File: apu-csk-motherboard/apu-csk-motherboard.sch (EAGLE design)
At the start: 11 parts

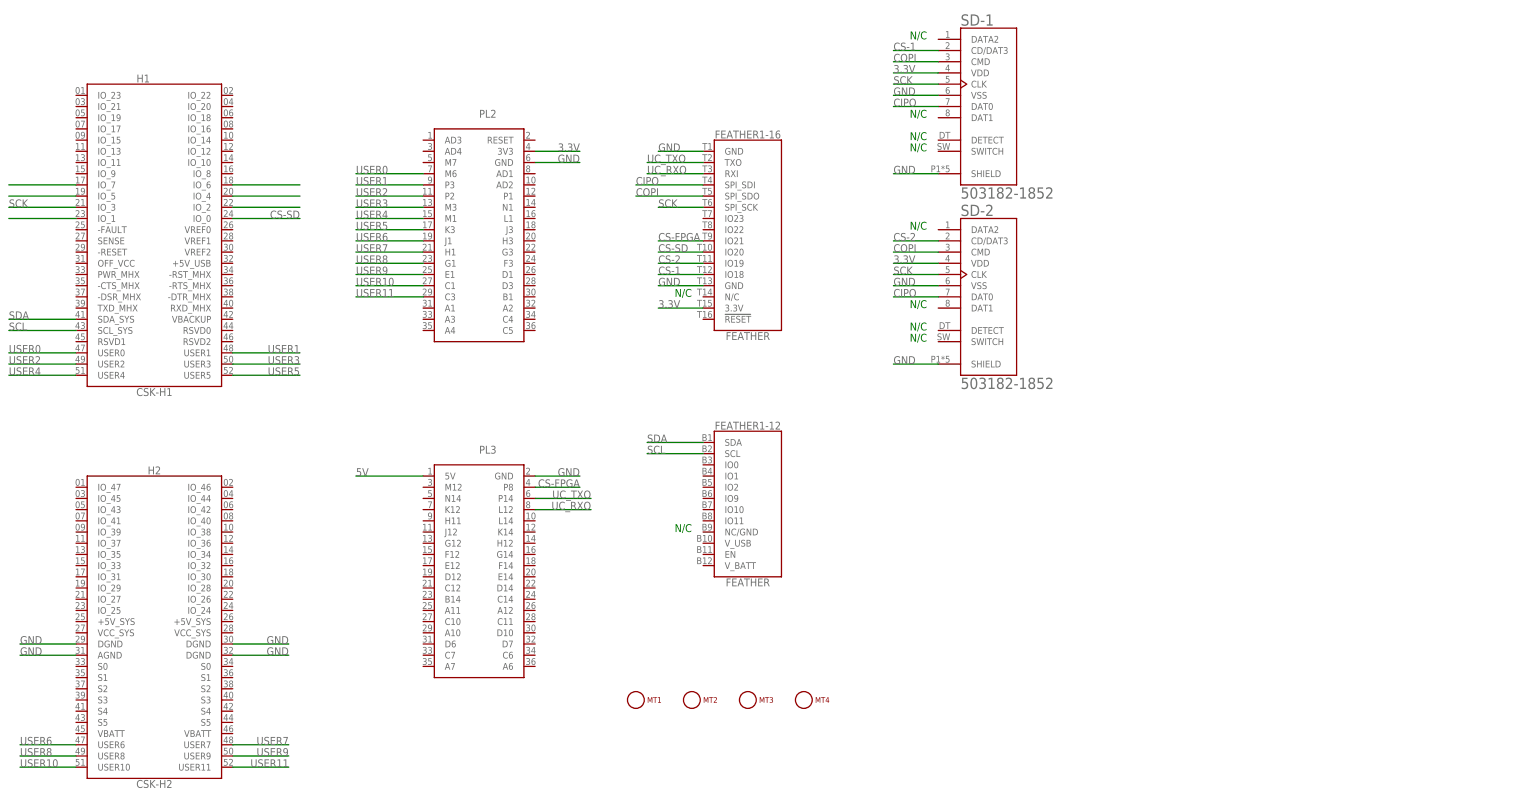
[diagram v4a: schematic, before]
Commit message: Added 4 temperature sensors, Authenitcation Chip, and Conncetors for RBF Switch
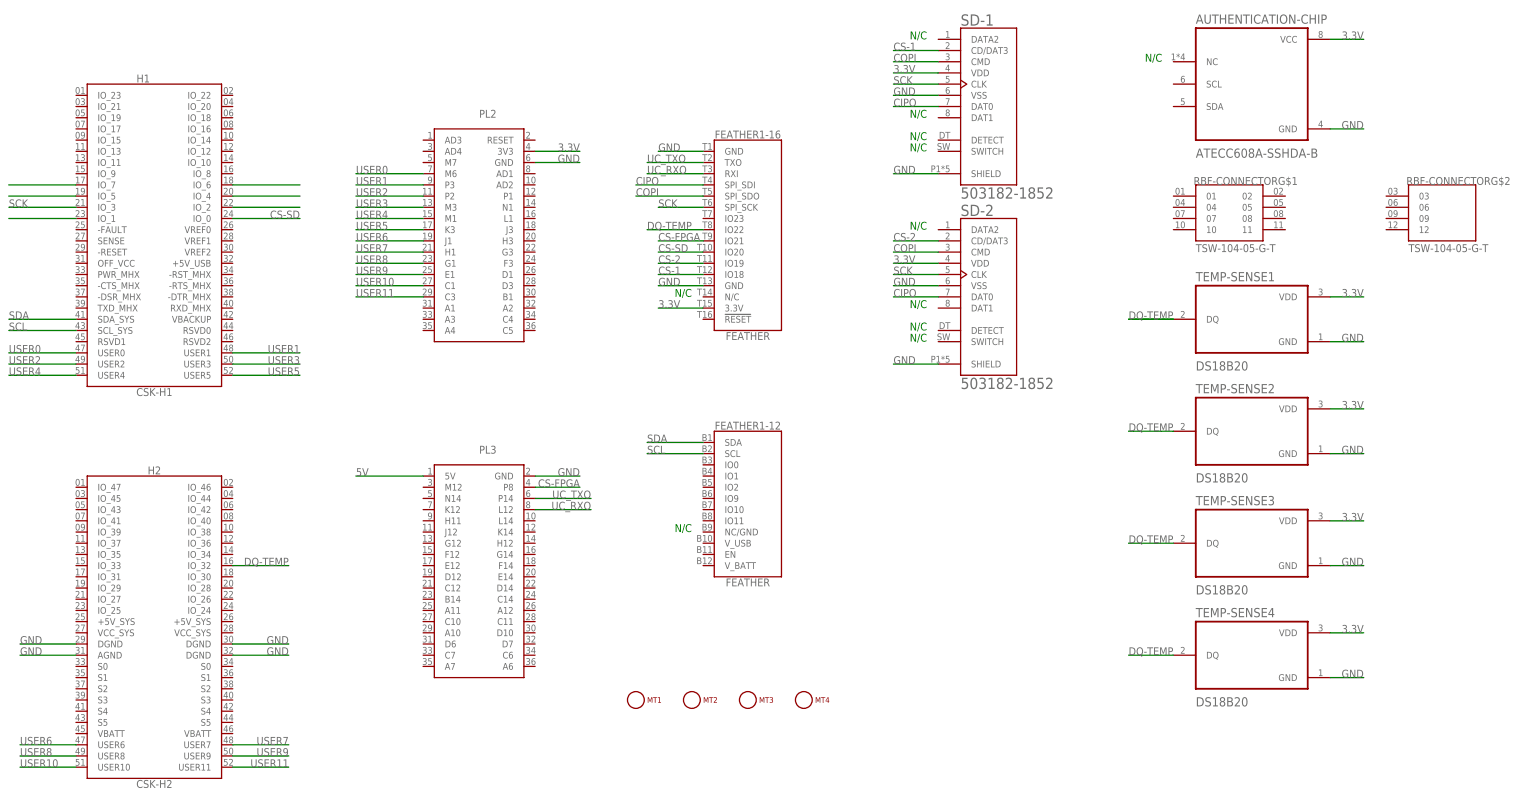
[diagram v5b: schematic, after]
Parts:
- added AUTHENTICATION-CHIP: ATECC608A-SSHDA-B, ATECC608A-SSHDA-B:ATECC608A-SSHDA-B
- added RBF-CONNECTOR: TSW-104-05-G-T, TSW-104-05-G-T:TSW-104-05-G-T
- added TEMP-SENSE1, TEMP-SENSE2, TEMP-SENSE3, TEMP-SENSE4: DS18B20, DS18B20:DS18B20
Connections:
- new net DQ-TEMP: FEATHER1-16.IO22@T8, H2.IO_32@16, TEMP-SENSE1.DQ, TEMP-SENSE2.DQ, TEMP-SENSE3.DQ, TEMP-SENSE4.DQ
- net 3.3V: now also AUTHENTICATION-CHIP.VCC, TEMP-SENSE1.VDD, TEMP-SENSE2.VDD, TEMP-SENSE3.VDD, TEMP-SENSE4.VDD
- net GND: now also AUTHENTICATION-CHIP.GND, TEMP-SENSE1.GND, TEMP-SENSE2.GND, TEMP-SENSE3.GND, TEMP-SENSE4.GND
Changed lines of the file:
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@@
 <part name="SD-1" library="503182-1852" deviceset="503182-1852" device=""/>
 <part name="SD-2" library="503182-1852" deviceset="503182-1852" device=""/>
+<part name="FRAME2" library="apu-csk-motherboard" deviceset="FRAME_LETTER_LANDSCAPE" device=""/>
+<part name="AUTHENTICATION-CHIP" library="ATECC608A-SSHDA-B" deviceset="ATECC608A-SSHDA-B" device=""/>
+<part name="RBF-CONNECTOR" library="TSW-104-05-G-T" deviceset="TSW-104-05-G-T" device=""/>
+<part name="TEMP-SENSE1" library="DS18B20" deviceset="DS18B20" device=""/>
+<part name="TEMP-SENSE2" library="DS18B20" deviceset="DS18B20" device=""/>
+<part name="TEMP-SENSE3" library="DS18B20" deviceset="DS18B20" device=""/>
+<part name="TEMP-SENSE4" library="DS18B20" deviceset="DS18B20" device=""/>
 </parts>
 <sheets>
@@
 <text x="218.44" y="114.3" size="1.778" layer="91" rot="MR0">N/C</text>
 <text x="218.44" y="111.76" size="1.778" layer="91" rot="MR0">N/C</text>
+<text x="271.78" y="175.26" size="1.778" layer="91" rot="MR0">N/C</text>
 </plain>
 <instances>
@@
 <attribute name="VALUE" x="226.06" y="101.025" size="2.548159375" layer="96"/>
 </instance>
+<instance part="FRAME2" gate="G$2" x="408.94" y="2.54" smashed="yes">
+<attribute name="LAST_DATE_TIME" x="421.64" y="3.81" size="2.54" layer="94"/>
+<attribute name="SHEET" x="495.3" y="3.81" size="2.54" layer="94"/>
+<attribute name="DRAWING_NAME" x="426.72" y="21.59" size="2.54" layer="94"/>
+</instance>
+<instance part="FRAME2" gate="G$1" x="261.62" y="2.54" smashed="yes"/>
+<instance part="AUTHENTICATION-CHIP" gate="G$1" x="292.1" y="170.18" smashed="yes">
+<attribute name="NAME" x="279.4" y="183.88" size="2.0828" layer="95" ratio="10" rot="SR0"/>
+<attribute name="VALUE" x="279.4" y="153.48" size="2.0828" layer="96" ratio="10" rot="SR0"/>
+</instance>
+<instance part="RBF-CONNECTOR" gate="G$1" x="287.02" y="139.7" smashed="yes">
+<attribute name="NAME" x="278.9" y="147.32" size="1.778" layer="95"/>
+<attribute name="VALUE" x="279.4" y="132.08" size="1.778" layer="96"/>
+</instance>
+<instance part="RBF-CONNECTOR" gate="G$2" x="335.28" y="139.7" smashed="yes">
+<attribute name="NAME" x="327.16" y="147.32" size="1.778" layer="95"/>
+<attribute name="VALUE" x="327.66" y="132.08" size="1.778" layer="96"/>
+</instance>
+<instance part="TEMP-SENSE1" gate="G$1" x="292.1" y="116.84" smashed="yes">
+<attribute name="NAME" x="279.4" y="125.46" size="2.0828" layer="95" ratio="10" rot="SR0"/>
+<attribute name="VALUE" x="279.4" y="105.22" size="2.0828" layer="96" ratio="10" rot="SR0"/>
+</instance>
+<instance part="TEMP-SENSE2" gate="G$1" x="292.1" y="91.44" smashed="yes">
+<attribute name="NAME" x="279.4" y="100.06" size="2.0828" layer="95" ratio="10" rot="SR0"/>
+<attribute name="VALUE" x="279.4" y="79.82" size="2.0828" layer="96" ratio="10" rot="SR0"/>
+</instance>
+<instance part="TEMP-SENSE3" gate="G$1" x="292.1" y="66.04" smashed="yes">
+<attribute name="NAME" x="279.4" y="74.66" size="2.0828" layer="95" ratio="10" rot="SR0"/>
+<attribute name="VALUE" x="279.4" y="54.42" size="2.0828" layer="96" ratio="10" rot="SR0"/>
+</instance>
+<instance part="TEMP-SENSE4" gate="G$1" x="292.1" y="40.64" smashed="yes">
+<attribute name="NAME" x="279.4" y="49.26" size="2.0828" layer="95" ratio="10" rot="SR0"/>
+<attribute name="VALUE" x="279.4" y="29.02" size="2.0828" layer="96" ratio="10" rot="SR0"/>
+</instance>
 </instances>
 <busses>
@@
 <label x="210.82" y="167.64" size="1.778" layer="95"/>
 </segment>
+<segment>
+<pinref part="TEMP-SENSE4" gate="G$1" pin="GND"/>
+<wire x1="317.5" y1="35.56" x2="309.88" y2="35.56" width="0.1524" layer="91"/>
+<label x="317.5" y="35.56" size="1.778" layer="95" rot="MR0"/>
+</segment>
+<segment>
+<pinref part="TEMP-SENSE3" gate="G$1" pin="GND"/>
+<wire x1="317.5" y1="60.96" x2="309.88" y2="60.96" width="0.1524" layer="91"/>
+<label x="317.5" y="60.96" size="1.778" layer="95" rot="MR0"/>
+</segment>
+<segment>
+<pinref part="TEMP-SENSE2" gate="G$1" pin="GND"/>
+<wire x1="317.5" y1="86.36" x2="309.88" y2="86.36" width="0.1524" layer="91"/>
+<label x="317.5" y="86.36" size="1.778" layer="95" rot="MR0"/>
+</segment>
+<segment>
+<pinref part="TEMP-SENSE1" gate="G$1" pin="GND"/>
+<wire x1="317.5" y1="111.76" x2="309.88" y2="111.76" width="0.1524" layer="91"/>
+<label x="317.5" y="111.76" size="1.778" layer="95" rot="MR0"/>
+</segment>
+<segment>
+<pinref part="AUTHENTICATION-CHIP" gate="G$1" pin="GND"/>
+<wire x1="317.5" y1="160.02" x2="309.88" y2="160.02" width="0.1524" layer="91"/>
+<label x="317.5" y="160.02" size="1.778" layer="95" rot="MR0"/>
+</segment>
 </net>
 <net name="3.3V" class="0">
@@
 <label x="210.82" y="172.72" size="1.778" layer="95"/>
 </segment>
+<segment>
+<pinref part="TEMP-SENSE1" gate="G$1" pin="VDD"/>
+<wire x1="309.88" y1="121.92" x2="317.5" y2="121.92" width="0.1524" layer="91"/>
+<label x="317.5" y="121.92" size="1.778" layer="95" rot="MR0"/>
+</segment>
+<segment>
+<pinref part="TEMP-SENSE2" gate="G$1" pin="VDD"/>
+<wire x1="317.5" y1="96.52" x2="309.88" y2="96.52" width="0.1524" layer="91"/>
+<label x="317.5" y="96.52" size="1.778" layer="95" rot="MR0"/>
+</segment>
+<segment>
+<pinref part="TEMP-SENSE3" gate="G$1" pin="VDD"/>
+<wire x1="317.5" y1="71.12" x2="309.88" y2="71.12" width="0.1524" layer="91"/>
+<label x="317.5" y="71.12" size="1.778" layer="95" rot="MR0"/>
+</segment>
+<segment>
+<pinref part="TEMP-SENSE4" gate="G$1" pin="VDD"/>
+<wire x1="317.5" y1="45.72" x2="309.88" y2="45.72" width="0.1524" layer="91"/>
+<label x="317.5" y="45.72" size="1.778" layer="95" rot="MR0"/>
+</segment>
+<segment>
+<pinref part="AUTHENTICATION-CHIP" gate="G$1" pin="VCC"/>
+<wire x1="317.5" y1="180.34" x2="309.88" y2="180.34" width="0.1524" layer="91"/>
+<label x="317.5" y="180.34" size="1.778" layer="95" rot="MR0"/>
+</segment>
 </net>
 <net name="SDA" class="0">
@@
 </segment>
 </net>
+<net name="DQ-TEMP" class="0">
+<segment>
+<pinref part="TEMP-SENSE1" gate="G$1" pin="DQ"/>
+<wire x1="264.16" y1="116.84" x2="274.32" y2="116.84" width="0.1524" layer="91"/>
+<label x="264.16" y="116.84" size="1.778" layer="95"/>
+<wire x1="264.16" y1="116.84" x2="274.32" y2="116.84" width="0.1524" layer="91"/>
+</segment>
+<segment>
+<pinref part="TEMP-SENSE2" gate="G$1" pin="DQ"/>
+<wire x1="264.16" y1="91.44" x2="274.32" y2="91.44" width="0.1524" layer="91"/>
+<label x="264.16" y="91.44" size="1.778" layer="95"/>
+</segment>
+<segment>
+<pinref part="TEMP-SENSE3" gate="G$1" pin="DQ"/>
+<wire x1="264.16" y1="66.04" x2="274.32" y2="66.04" width="0.1524" layer="91"/>
+<label x="264.16" y="66.04" size="1.778" layer="95"/>
+</segment>
+<segment>
+<pinref part="TEMP-SENSE4" gate="G$1" pin="DQ"/>
+<wire x1="264.16" y1="40.64" x2="274.32" y2="40.64" width="0.1524" layer="91"/>
+<label x="264.16" y="40.64" size="1.778" layer="95"/>
+</segment>
+<segment>
+<pinref part="FEATHER1" gate="-16" pin="IO22@T8"/>
+<wire x1="154.94" y1="137.16" x2="167.64" y2="137.16" width="0.1524" layer="91"/>
+<label x="154.94" y="137.16" size="1.778" layer="95"/>
+</segment>
+<segment>
+<pinref part="H2" gate="G$1" pin="IO_32@16"/>
+<wire x1="60.96" y1="60.96" x2="73.66" y2="60.96" width="0.1524" layer="91"/>
+<label x="73.66" y="60.96" size="1.778" layer="95" rot="MR0"/>
+</segment>
+</net>

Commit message: Added the components to a second sheet and finished wiring the authenticator chip
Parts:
- removed RBF-CONNECTOR: TSW-104-05-G-T, TSW-104-05-G-T:TSW-104-05-G-T
- added LAUNCH-SW-CN: TSW-104-05-G-T, TSW-104-05-G-T:TSW-104-05-G-T
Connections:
- net CS-1 renamed CS-SD-1
- net CS-2 renamed CS-SD-2
- new net LSW-1-C: LAUNCH-SW-CNG$2.03
- new net LSW-1-NC: LAUNCH-SW-CNG$1.01
- new net LSW-1-NO: LAUNCH-SW-CNG$1.02
- new net LSW-2-C: LAUNCH-SW-CNG$2.06
- new net LSW-2-NC: LAUNCH-SW-CNG$1.04
- new net LSW-2-NO: LAUNCH-SW-CNG$1.05
- new net LSW-3-C: LAUNCH-SW-CNG$2.09
- new net LSW-3-NC: LAUNCH-SW-CNG$1.07
- new net LSW-3-NO: LAUNCH-SW-CNG$1.08
- new net LSW-4-C: LAUNCH-SW-CNG$2.12
- new net LSW-4-NC: LAUNCH-SW-CNG$1.10
- new net LSW-4-NO: LAUNCH-SW-CNG$1.11
- net CS-SD: no longer FEATHER1-16.IO20@T10
- net SCL: now also AUTHENTICATION-CHIP.SCL
- net SDA: now also AUTHENTICATION-CHIP.SDA
